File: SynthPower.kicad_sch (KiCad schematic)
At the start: 29 parts, among them J29 Conn_01x16_Pin, J44 Jack-DC, J45 Conn_01x10_Pin, U50 BUF634AIDDAR, U53 TPS560200, U54 LM1117MP-3.3

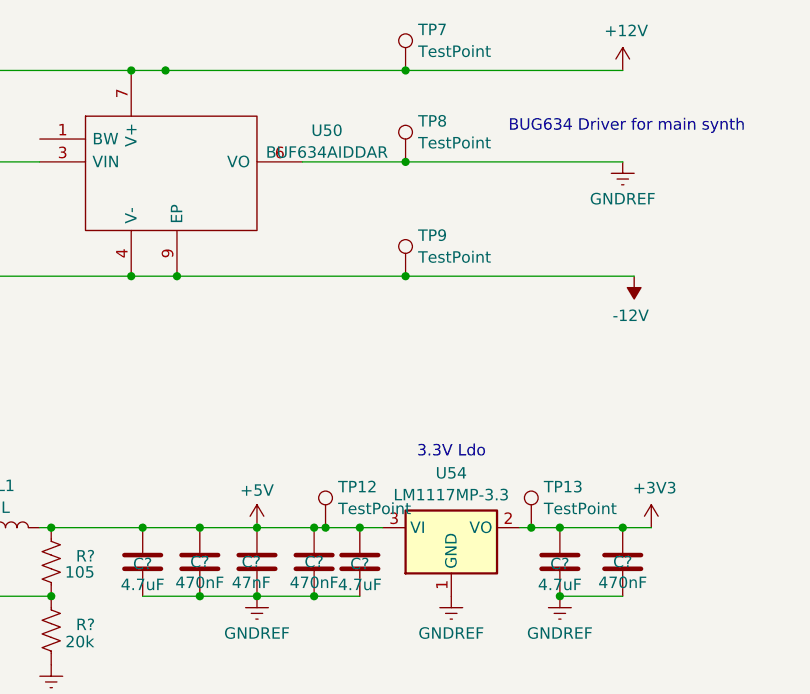
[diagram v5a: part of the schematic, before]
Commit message: routing microcontroller
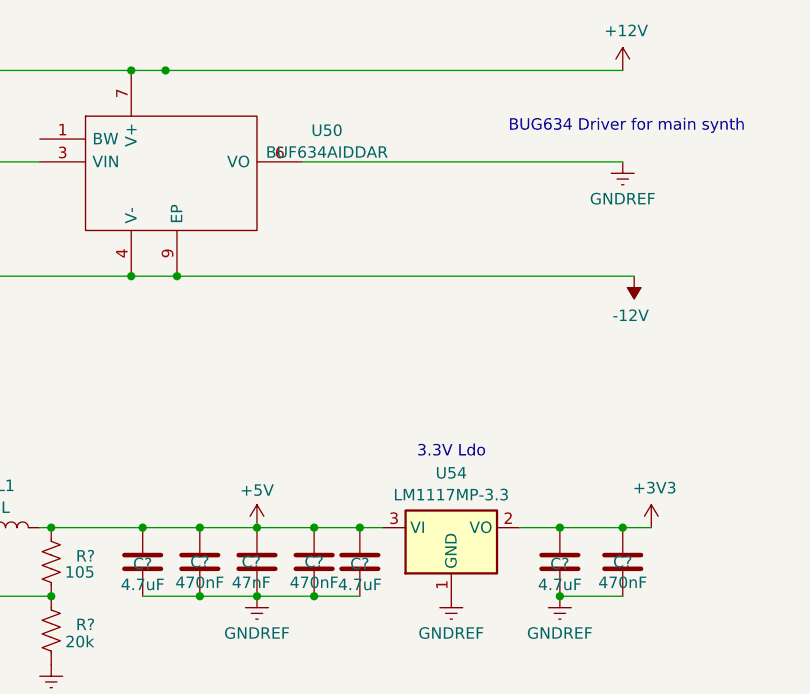
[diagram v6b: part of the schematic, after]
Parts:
- removed TP12, TP13, TP7, TP8, TP9: TestPoint, TestPoint:TestPoint_Plated_Hole_D2.0mm, symbol Connector:TestPoint
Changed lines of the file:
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@@
   (junction (at 103.505 60.96) (diameter 0) (color 0 0 0 0)
   )
-  (junction (at 128.905 38.1) (diameter 0) (color 0 0 0 0)
-  )
-  (junction (at 128.905 48.26) (diameter 0) (color 0 0 0 0)
-  )
   (junction (at 106.045 135.89) (diameter 0) (color 0 0 0 0)
   )
@@
   (junction (at 67.945 55.88) (diameter 0) (color 0 0 0 0)
   )
-  (junction (at 128.905 60.96) (diameter 0) (color 0 0 0 0)
-  )
   (junction (at 186.69 57.785) (diameter 0) (color 0 0 0 0)
   )
@@
   (junction (at 60.325 132.08) (diameter 0) (color 0 0 0 0)
   )
-  (junction (at 120.015 88.9) (diameter 0) (color 0 0 0 0)
-  )
-  (junction (at 142.875 88.9) (diameter 0) (color 0 0 0 0)
-  )
   (junction (at 50.165 55.88) (diameter 0) (color 0 0 0 0)
   )
@@
     (stroke (width 0) (type default))
   )
-  (wire (pts (xy 118.745 88.9) (xy 120.015 88.9))
+  (wire (pts (xy 118.745 88.9) (xy 123.825 88.9))
     (stroke (width 0) (type default))
   )
@@
     (stroke (width 0) (type default))
   )
-  (wire (pts (xy 120.015 88.9) (xy 123.825 88.9))
-    (stroke (width 0) (type default))
-  )
-  (wire (pts (xy 102.235 38.1) (xy 128.905 38.1))
+  (wire (pts (xy 102.235 38.1) (xy 153.035 38.1))
     (stroke (width 0) (type default))
   )
@@
     (stroke (width 0) (type default))
   )
-  (wire (pts (xy 142.875 88.9) (xy 141.605 88.9))
+  (wire (pts (xy 141.605 88.9) (xy 146.05 88.9))
     (stroke (width 0) (type default))
   )
@@
     (stroke (width 0) (type default))
   )
-  (wire (pts (xy 128.905 48.26) (xy 153.035 48.26))
-    (stroke (width 0) (type default))
-  )
   (wire (pts (xy 88.265 88.9) (xy 89.535 88.9))
     (stroke (width 0) (type default))
@@
     (stroke (width 0) (type default))
   )
-  (wire (pts (xy 128.905 38.1) (xy 153.035 38.1))
-    (stroke (width 0) (type default))
-  )
   (wire (pts (xy 98.425 60.96) (xy 103.505 60.96))
     (stroke (width 0) (type default))
@@
     (stroke (width 0) (type default))
   )
-  (wire (pts (xy 128.905 60.96) (xy 154.305 60.96))
-    (stroke (width 0) (type default))
-  )
   (wire (pts (xy 193.04 57.785) (xy 199.39 57.785))
     (stroke (width 0) (type default))
@@
     (stroke (width 0) (type default))
   )
-  (wire (pts (xy 103.505 60.96) (xy 128.905 60.96))
+  (wire (pts (xy 103.505 60.96) (xy 154.305 60.96))
     (stroke (width 0) (type default))
   )
@@
     (stroke (width 0) (type default))
   )
-  (wire (pts (xy 146.05 88.9) (xy 142.875 88.9))
-    (stroke (width 0) (type default))
-  )
   (wire (pts (xy 106.045 123.19) (xy 121.92 123.19))
     (stroke (width 0) (type default))
@@
     (stroke (width 0) (type default))
   )
-  (wire (pts (xy 117.475 48.26) (xy 128.905 48.26))
+  (wire (pts (xy 117.475 48.26) (xy 153.035 48.26))
     (stroke (width 0) (type default))
   )
@@
         (path "/9021c97e-351f-4ed9-b393-50257df6a463/b7926a34-b39e-4f5f-b85d-b7e065fdd5f5"
           (reference "R405") (unit 1)
-        )
-      )
-    )
-  )
-  (symbol (lib_id "Connector:TestPoint") (at 128.905 60.96 0) (unit 1)
-    (in_bom yes) (on_board yes) (dnp no) (fields_autoplaced)
-    (property "Reference" "TP9" (at 130.302 56.4459 0)
-      (effects (font (size 1.27 1.27)) (justify left))
-    )
-    (property "Value" "TestPoint" (at 130.302 58.8701 0)
-      (effects (font (size 1.27 1.27)) (justify left))
-    )
-    (property "Footprint" "TestPoint:TestPoint_Plated_Hole_D2.0mm" (at 133.985 60.96 0)
-      (effects (font (size 1.27 1.27)) hide)
-    )
-    (property "Datasheet" "~" (at 133.985 60.96 0)
-      (effects (font (size 1.27 1.27)) hide)
-    )
-    (pin "1")
-    (instances
-      (project "SynthProj"
-        (path "/9021c97e-351f-4ed9-b393-50257df6a463/b7926a34-b39e-4f5f-b85d-b7e065fdd5f5"
-          (reference "TP9") (unit 1)
         )
       )
@@
     )
   )
-  (symbol (lib_id "Connector:TestPoint") (at 120.015 88.9 0) (unit 1)
-    (in_bom yes) (on_board yes) (dnp no) (fields_autoplaced)
-    (property "Reference" "TP12" (at 121.412 84.3859 0)
-      (effects (font (size 1.27 1.27)) (justify left))
-    )
-    (property "Value" "TestPoint" (at 121.412 86.8101 0)
-      (effects (font (size 1.27 1.27)) (justify left))
-    )
-    (property "Footprint" "TestPoint:TestPoint_Plated_Hole_D2.0mm" (at 125.095 88.9 0)
-      (effects (font (size 1.27 1.27)) hide)
-    )
-    (property "Datasheet" "~" (at 125.095 88.9 0)
-      (effects (font (size 1.27 1.27)) hide)
-    )
-    (pin "1")
-    (instances
-      (project "SynthProj"
-        (path "/9021c97e-351f-4ed9-b393-50257df6a463/b7926a34-b39e-4f5f-b85d-b7e065fdd5f5"
-          (reference "TP12") (unit 1)
-        )
-      )
-    )
-  )
   (symbol (lib_id "BUF634AIDDAR:BUF634AIDDAR") (at 103.505 48.26 0) (unit 1)
     (in_bom yes) (on_board yes) (dnp no) (fields_autoplaced)
@@
     )
   )
-  (symbol (lib_id "Connector:TestPoint") (at 128.905 38.1 0) (unit 1)
-    (in_bom yes) (on_board yes) (dnp no) (fields_autoplaced)
-    (property "Reference" "TP7" (at 130.302 33.5859 0)
-      (effects (font (size 1.27 1.27)) (justify left))
-    )
-    (property "Value" "TestPoint" (at 130.302 36.0101 0)
-      (effects (font (size 1.27 1.27)) (justify left))
-    )
-    (property "Footprint" "TestPoint:TestPoint_Plated_Hole_D2.0mm" (at 133.985 38.1 0)
-      (effects (font (size 1.27 1.27)) hide)
-    )
-    (property "Datasheet" "~" (at 133.985 38.1 0)
-      (effects (font (size 1.27 1.27)) hide)
-    )
-    (pin "1")
-    (instances
-      (project "SynthProj"
-        (path "/9021c97e-351f-4ed9-b393-50257df6a463/b7926a34-b39e-4f5f-b85d-b7e065fdd5f5"
-          (reference "TP7") (unit 1)
-        )
-      )
-    )
-  )
   (symbol (lib_id "power:GNDREF") (at 112.395 96.52 0) (unit 1)
     (in_bom yes) (on_board yes) (dnp no) (fields_autoplaced)
@@
     )
   )
-  (symbol (lib_id "Connector:TestPoint") (at 142.875 88.9 0) (unit 1)
-    (in_bom yes) (on_board yes) (dnp no) (fields_autoplaced)
-    (property "Reference" "TP13" (at 144.272 84.3859 0)
-      (effects (font (size 1.27 1.27)) (justify left))
-    )
-    (property "Value" "TestPoint" (at 144.272 86.8101 0)
-      (effects (font (size 1.27 1.27)) (justify left))
-    )
-    (property "Footprint" "TestPoint:TestPoint_Plated_Hole_D2.0mm" (at 147.955 88.9 0)
-      (effects (font (size 1.27 1.27)) hide)
-    )
-    (property "Datasheet" "~" (at 147.955 88.9 0)
-      (effects (font (size 1.27 1.27)) hide)
-    )
-    (pin "1")
-    (instances
-      (project "SynthProj"
-        (path "/9021c97e-351f-4ed9-b393-50257df6a463/b7926a34-b39e-4f5f-b85d-b7e065fdd5f5"
-          (reference "TP13") (unit 1)
-        )
-      )
-    )
-  )
   (symbol (lib_id "Device:R_US") (at 89.535 92.71 0) (unit 1)
     (in_bom yes) (on_board yes) (dnp no)
@@
         )
       )
-    )
-  )
-  (symbol (lib_id "Connector:TestPoint") (at 128.905 48.26 0) (unit 1)
-    (in_bom yes) (on_board yes) (dnp no) (fields_autoplaced)
-    (property "Reference" "TP8" (at 130.302 43.7459 0)
-      (effects (font (size 1.27 1.27)) (justify left))
-    )
-    (property "Value" "TestPoint" (at 130.302 46.1701 0)
-      (effects (font (size 1.27 1.27)) (justify left))
-    )
-    (property "Footprint" "TestPoint:TestPoint_Plated_Hole_D2.0mm" (at 133.985 48.26 0)
-      (effects (font (size 1.27 1.27)) hide)
-    )
-    (property "Datasheet" "~" (at 133.985 48.26 0)
-      (effects (font (size 1.27 1.27)) hide)
-    )
-    (pin "1")
-    (instances
-      (project "SynthProj"
-        (path "/9021c97e-351f-4ed9-b393-50257df6a463/b7926a34-b39e-4f5f-b85d-b7e065fdd5f5"
-          (reference "TP8") (unit 1)
-        )
-      )

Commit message: more and more and more and more and more routing
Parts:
- removed J45: Conn_01x10_Pin, symbol Connector:Conn_01x10_Pin
- added D1: 1N914, Diode_SMD:D_SOD-323F, symbol Diode:1N914
- J29: footprint (none) -> Connector_PinHeader_2.54mm:PinHeader_2x08_P2.54mm_Vertical
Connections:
- net +5V: now also D1.1 (K)
- new net VBUS: D1.2 (A)
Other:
- note added: "EuroRack Power Header"
- note removed: "EuroRack Power Headers"
- moved on the sheet: J29
